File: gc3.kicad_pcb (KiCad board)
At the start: 6 copper layers, 99.1 x 66.8 mm, 191 parts, among them J1 JACK, J2 DM3AT-SF-PEJM5, P1 TESTPOINT, P10 UART1, P11 GND, P12 GND, P13 GND, P14 GND, P15 TESTPOINT, P16 TEESTPOINT, P17 GPIO, P18 USB_A, P19 USB_OTG, P2 TESTPOINT, P3 TESTPOINT, P4 TESTPOINT, P5 TESTPOINT, P6 TESTPOINT, P7 LCD, P8 JTAG, P9 UART0, SW1 PWR_ON, SW2 RESET, SW3 UBOOT, U1 TPS62290, U2 axp209, U3 TPS62290, U4 a13, U5 h5tq2g63bfr, U6 TPS2552, U8 TPS2552, Y1 24MHz/20pF/20ppm

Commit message: Add : finish Update$
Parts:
- C29, C30, C32, C33, C34, C35, C36, C38, C39, C40, C41, C42, C43, C44, C47, C48, C49, C66, C80, C81: footprint COMMON0603:Common_0603 -> Capacitors_SMD:C_0402
- C50: footprint COMMON0603:Common_0603 -> Capacitors_SMD:C_0402; moved to B.Cu
- C82: moved to B.Cu
- R19, R26, R66, R74: footprint COMMON0603:Common_0603 -> Resistors_SMD:R_0402
- moved R19 7.04 mm to (163.1, 109.0)
- moved C80 6.78 mm to (163.0, 107.6)
- moved R74 6.69 mm to (163.1, 106.3)
- moved C81 6.47 mm to (163.0, 105.0)
- moved C66 6.34 mm to (163.0, 103.7)
- moved C50 4.40 mm to (174.9, 83.4), turned to 180 degrees
- moved C35 4.25 mm to (152.7, 91.0)
- moved P15 3.86 mm to (144.7, 78.7)
- moved P16 3.60 mm to (124.0, 119.4)
- moved C1 3.35 mm to (123.0, 115.6)
- moved C33 2.34 mm to (148.8, 90.0)
- moved P14 2.04 mm to (129.1, 121.4)
- moved C72 2.00 mm to (166.2, 111.5), turned to 270 degrees
- moved C30 1.57 mm to (173.3, 68.7)
- moved C34 1.44 mm to (152.6, 87.8)
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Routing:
- net +5V: track 38.4 -> 170.0 mm
- net +1.5V: track 51.1 -> 109.5 mm, vias 17 -> 23
- net +3V3: track 47.5 -> 72.4 mm, vias 0 -> 19
- net GND: track 225.9 -> 244.1 mm, vias 102 -> 113
- net +3.0VA: track 72.0 -> 86.8 mm, vias 3 -> 4
- net IPSOUT: track 125.6 -> 137.1 mm, vias 14 -> 15
- net 1.2V_INT: track 30.6 -> 38.5 mm, vias 0 -> 7
- net /mpu_ddr3/SVREF: track 18.5 -> 11.2 mm
- net /mpu_ddr3/PIN39/USBH_EN: track 131.0 -> 123.7 mm
- net /mpu_ddr3/PIN8: track 80.2 -> 84.4 mm
- net /mpu_ddr3/DQS1_N: track 15.9 -> 11.8 mm
- net /mpu_ddr3/D15: track 14.2 -> 11.3 mm
- net /mpu_ddr3/A4: track 16.8 -> 19.3 mm
- net Net-(D2-Pad2): track 0.00 -> 2.58 mm
- net /mpu_ddr3/CK_N: track 22.1 -> 20.0 mm
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
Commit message: Commit before production Update4
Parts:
- added ?: , via:via, F.Cu at (185.6, 64.9)
- added ?: , via:via, F.Cu at (141.4, 84.9)
- added ?: , via:via, F.Cu at (109.1, 63.1)
- added ?: , via:via, F.Cu at (109.1, 58.9)
- added ?: , via:via, F.Cu at (112.4, 58.9)
- added ?: , via:via, F.Cu at (115.7, 58.9)
- added ?: , via:via, F.Cu at (118.7, 58.8)
- added ?: , via:via, F.Cu at (122.2, 58.8)
- added ?: , via:via, F.Cu at (128.1, 58.8)
- added ?: , via:via, F.Cu at (133.1, 67.0)
- added ?: , via:via, F.Cu at (131.3, 63.0)
- added ?: , via:via, F.Cu at (132.4, 58.8)
- added ?: , via:via, F.Cu at (137.0, 84.3)
- added ?: , via:via, F.Cu at (144.1, 65.0)
- added ?: , via:via, F.Cu at (137.0, 58.8)
- added ?: , via:via, F.Cu at (146.7, 58.8)
- added ?: , via:via, F.Cu at (144.3, 112.4)
- added ?: , via:via, F.Cu at (144.3, 107.1)
- added ?: , via:via, F.Cu at (155.1, 115.3)
- added ?: , via:via, F.Cu at (155.0, 112.1)
- added ?: , via:via, F.Cu at (158.9, 110.4)
- added ?: , via:via, F.Cu at (151.9, 114.1)
- added ?: , via:via, F.Cu at (152.0, 111.9)
- added ?: , via:via, F.Cu at (134.6, 107.1)
- added ?: , via:via, F.Cu at (151.9, 109.6)
- added ?: , via:via, F.Cu at (144.4, 108.9)
- added ?: , via:via, F.Cu at (162.7, 101.2)
- added ?: , via:via, F.Cu at (160.5, 103.5)
- added ?: , via:via, F.Cu at (159.4, 105.6)
- added ?: , via:via, F.Cu at (155.1, 104.5)
- added ?: , via:via, F.Cu at (155.1, 107.1)
- added ?: , via:via, F.Cu at (151.9, 107.2)
- added ?: , via:via, F.Cu at (188.8, 117.8)
- added ?: , via:via, F.Cu at (192.8, 119.3)
- added ?: , via:via, F.Cu at (135.3, 99.7)
- added ?: , via:via, F.Cu at (193.3, 121.7)
- added ?: , via:via, F.Cu at (192.7, 124.0)
- added ?: , via:via, F.Cu at (197.8, 121.0)
- added ?: , via:via, F.Cu at (192.3, 117.2)
- added ?: , via:via, F.Cu at (185.4, 113.6)
- added ?: , via:via, F.Cu at (190.3, 112.0)
- added ?: , via:via, F.Cu at (198.3, 115.2)
- added ?: , via:via, F.Cu at (201.4, 108.2)
- added ?: , via:via, F.Cu at (195.3, 108.6)
- added ?: , via:via, F.Cu at (189.1, 105.7)
- added ?: , via:via, F.Cu at (143.7, 99.7)
- added ?: , via:via, F.Cu at (192.4, 102.0)
- added ?: , via:via, F.Cu at (199.2, 103.2)
- added ?: , via:via, F.Cu at (206.7, 124.0)
- added ?: , via:via, F.Cu at (206.5, 121.7)
- added ?: , via:via, F.Cu at (206.5, 117.4)
- added ?: , via:via, F.Cu at (206.5, 112.8)
- added ?: , via:via, F.Cu at (206.6, 108.0)
- added ?: , via:via, F.Cu at (206.6, 101.4)
- added ?: , via:via, F.Cu at (202.6, 97.9)
- added ?: , via:via, F.Cu at (195.4, 97.3)
- added ?: , via:via, F.Cu at (168.6, 102.0)
- added ?: , via:via, F.Cu at (188.2, 97.6)
- added ?: , via:via, F.Cu at (176.9, 77.3)
- added ?: , via:via, F.Cu at (183.9, 113.3)
- added ?: , via:via, F.Cu at (185.1, 95.4)
- added ?: , via:via, F.Cu at (185.1, 89.1)
- added ?: , via:via, F.Cu at (151.2, 58.9)
- added ?: , via:via, F.Cu at (177.9, 83.4)
- added ?: , via:via, F.Cu at (185.1, 92.0)
- added ?: , via:via, F.Cu at (185.1, 98.5)
- added ?: , via:via, F.Cu at (185.3, 84.9)
- added ?: , via:via, F.Cu at (134.4, 114.9)
- added ?: , via:via, F.Cu at (188.0, 87.6)
- added ?: , via:via, F.Cu at (190.9, 96.1)
- added ?: , via:via, F.Cu at (199.3, 94.8)
- added ?: , via:via, F.Cu at (206.6, 94.7)
- added ?: , via:via, F.Cu at (190.1, 83.3)
- added ?: , via:via, F.Cu at (206.6, 72.1)
- added ?: , via:via, F.Cu at (206.6, 79.3)
- added ?: , via:via, F.Cu at (202.0, 79.1)
- added ?: , via:via, F.Cu at (197.3, 79.4)
- added ?: , via:via, F.Cu at (193.0, 77.4)
- added ?: , via:via, F.Cu at (133.8, 111.5)
- added ?: , via:via, F.Cu at (206.6, 87.5)
- added ?: , via:via, F.Cu at (199.3, 75.2)
- added ?: , via:via, F.Cu at (204.8, 75.7)
- added ?: , via:via, F.Cu at (203.3, 72.0)
- added ?: , via:via, F.Cu at (200.7, 67.8)
- added ?: , via:via, F.Cu at (194.5, 70.2)
- added ?: , via:via, F.Cu at (190.0, 70.0)
- added ?: , via:via, F.Cu at (154.1, 58.9)
- added ?: , via:via, F.Cu at (190.4, 66.5)
- added ?: , via:via, F.Cu at (191.8, 64.1)
- added ?: , via:via, F.Cu at (132.9, 112.2)
- added ?: , via:via, F.Cu at (191.7, 60.9)
- added ?: , via:via, F.Cu at (194.9, 62.4)
- added ?: , via:via, F.Cu at (182.7, 58.9)
- added ?: , via:via, F.Cu at (197.9, 58.8)
- added ?: , via:via, F.Cu at (193.7, 58.8)
- added ?: , via:via, F.Cu at (202.9, 58.7)
- added ?: , via:via, F.Cu at (199.7, 63.3)
- added ?: , via:via, F.Cu at (206.3, 63.5)
- added ?: , via:via, F.Cu at (176.9, 98.5)
- added ?: , via:via, F.Cu at (206.7, 58.7)
- added ?: , via:via, F.Cu at (135.6, 111.8)
- added ?: , via:via, F.Cu at (188.5, 68.5)
- added ?: , via:via, F.Cu at (182.8, 64.8)
- added ?: , via:via, F.Cu at (143.6, 103.8)
- added ?: , via:via, F.Cu at (137.4, 107.2)
- added ?: , via:via, F.Cu at (141.3, 107.2)
- added ?: , via:via, F.Cu at (141.6, 111.6)
- added ?: , via:via, F.Cu at (138.5, 108.8)
- added ?: , via:via, F.Cu at (142.9, 113.8)
- added ?: , via:via, F.Cu at (140.9, 118.0)
- added ?: , via:via, F.Cu at (132.8, 120.0)
- added ?: , via:via, F.Cu at (131.0, 115.8)
- added ?: , via:via, F.Cu at (126.9, 117.3)
- added ?: , via:via, F.Cu at (180.6, 67.0)
- added ?: , via:via, F.Cu at (125.0, 110.7)
- added ?: , via:via, F.Cu at (127.9, 111.4)
- added ?: , via:via, F.Cu at (128.0, 107.1)
- added ?: , via:via, F.Cu at (126.0, 107.2)
- added ?: , via:via, F.Cu at (123.6, 107.1)
- added ?: , via:via, F.Cu at (121.8, 118.0)
- added ?: , via:via, F.Cu at (135.2, 123.9)
- added ?: , via:via, F.Cu at (131.2, 123.9)
- added ?: , via:via, F.Cu at (124.1, 123.9)
- added ?: , via:via, F.Cu at (119.7, 123.9)
- added ?: , via:via, F.Cu at (183.4, 67.0)
- added ?: , via:via, F.Cu at (114.7, 123.9)
- added ?: , via:via, F.Cu at (112.5, 119.2)
- added ?: , via:via, F.Cu at (115.7, 117.7)
- added ?: , via:via, F.Cu at (113.9, 113.3)
- added ?: , via:via, F.Cu at (112.8, 110.4)
- added ?: , via:via, F.Cu at (111.3, 106.5)
- added ?: , via:via, F.Cu at (109.2, 123.9)
- added ?: , via:via, F.Cu at (109.1, 121.4)
- added ?: , via:via, F.Cu at (109.1, 117.5)
- added ?: , via:via, F.Cu at (109.1, 114.2)
- added ?: , via:via, F.Cu at (136.4, 90.4)
- added ?: , via:via, F.Cu at (109.1, 110.1)
- added ?: , via:via, F.Cu at (120.6, 91.1)
- added ?: , via:via, F.Cu at (112.7, 96.0)
- added ?: , via:via, F.Cu at (109.2, 95.4)
- added ?: , via:via, F.Cu at (109.2, 93.8)
- added ?: , via:via, F.Cu at (111.2, 89.1)
- added ?: , via:via, F.Cu at (109.1, 89.2)
- added ?: , via:via, F.Cu at (109.1, 86.4)
- added ?: , via:via, F.Cu at (111.4, 78.8)
- added ?: , via:via, F.Cu at (111.4, 73.0)
- added ?: , via:via, F.Cu at (142.3, 94.5)
- added ?: , via:via, F.Cu at (109.2, 79.6)
- added ?: , via:via, F.Cu at (109.1, 74.7)
- added ?: , via:via, F.Cu at (109.1, 70.1)
- added ?: , via:via, F.Cu at (113.0, 71.2)
- added ?: , via:via, F.Cu at (113.0, 66.9)
- added ?: , via:via, F.Cu at (111.7, 65.7)
- added ?: , via:via, F.Cu at (109.1, 66.3)
- added ?: , via:via, F.Cu at (125.2, 82.1)
- added ?: , via:via, F.Cu at (114.6, 87.5)
- added ?: , via:via, F.Cu at (113.9, 87.6)
- added ?: , via:via, F.Cu at (139.6, 94.5)
- added ?: , via:via, F.Cu at (113.8, 82.0)
- added ?: , via:via, F.Cu at (115.6, 83.7)
- added ?: , via:via, F.Cu at (117.9, 83.8)
- added ?: , via:via, F.Cu at (120.9, 84.5)
- added ?: , via:via, F.Cu at (127.1, 86.2)
- added ?: , via:via, F.Cu at (123.3, 83.2)
- added ?: , via:via, F.Cu at (120.1, 81.3)
- added ?: , via:via, F.Cu at (116.8, 81.3)
- added ?: , via:via, F.Cu at (125.1, 79.1)
- added ?: , via:via, F.Cu at (129.6, 79.1)
- added ?: , via:via, F.Cu at (143.2, 88.9)
- added ?: , via:via, F.Cu at (129.7, 74.5)
- added ?: , via:via, F.Cu at (128.2, 71.4)
- added ?: , via:via, F.Cu at (137.5, 75.3)
- added ?: , via:via, F.Cu at (137.7, 76.2)
- added ?: , via:via, F.Cu at (140.9, 74.8)
- added ?: , via:via, F.Cu at (145.5, 74.5)
- added ?: , via:via, F.Cu at (143.7, 72.2)
- added ?: , via:via, F.Cu at (143.7, 69.0)
- added ?: , via:via, F.Cu at (141.9, 68.4)
- added ?: , via:via, F.Cu at (149.9, 69.5)
- added ?: , via:via, F.Cu at (145.2, 86.8)
- added ?: , via:via, F.Cu at (147.2, 70.1)
- added ?: , via:via, F.Cu at (146.1, 71.9)
- added ?: , via:via, F.Cu at (139.2, 71.5)
- added ?: , via:via, F.Cu at (131.5, 69.2)
- added ?: , via:via, F.Cu at (123.5, 69.2)
- added ?: , via:via, F.Cu at (128.1, 66.1)
- added ?: , via:via, F.Cu at (121.3, 64.9)
- added ?: , via:via, F.Cu at (119.4, 61.6)
- added ?: , via:via, F.Cu at (114.9, 70.4)
- added ?: , via:via, F.Cu at (114.3, 63.3)
- moved C66 3.03 mm to (163.1, 106.7)
- moved R66 2.91 mm to (162.8, 105.0)
- moved C81 2.74 mm to (163.1, 107.7)
- moved R74 2.41 mm to (163.2, 108.7)
- moved C80 2.07 mm to (163.1, 109.7)
- moved R19 1.70 mm to (163.2, 110.7)
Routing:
- net GND: track 244.1 -> 298.2 mm, vias 113 -> 122
- net /mpu_ddr3/DQS1_N: track 11.8 -> 16.0 mm
- net /mpu_ddr3/DM0: track 12.4 -> 16.1 mm
- net /mpu_ddr3/BA1: track 15.6 -> 19.0 mm
- net /mpu_ddr3/DM1: track 11.5 -> 14.5 mm
- net Net-(R66-Pad2): track 4.43 -> 7.18 mm
- net /mpu_ddr3/A4: track 19.3 -> 16.7 mm
- net +1.5V: track 109.5 -> 107.2 mm
- net /mpu_ddr3/SVREF: track 11.2 -> 12.9 mm
- net +3V3: track 72.4 -> 70.9 mm
- net /mpu_ddr3/DQS1_P: track 15.1 -> 16.1 mm
- net /mpu_ddr3/PIN13/NALE: track 23.9 -> 24.8 mm
- net /mpu_ddr3/PIN14/NCLE: track 23.4 -> 24.3 mm
- net /mpu_ddr3/PIN12/NWE: track 25.3 -> 26.2 mm
- net /EXTEN: track 24.2 -> 23.4 mm
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- added copper zone on In1.Cu, net GND
- added copper zone on In2.Cu, net GND

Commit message: temp : commit before change 8 layer
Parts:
- moved C30 1.93 mm to (171.8, 69.8)
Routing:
- net GND: track 298.2 -> 329.0 mm, vias 122 -> 125
- net +3V3: track 70.9 -> 67.0 mm
- net PIN5/TWI0-SDA: track 125.2 -> 121.7 mm
- net Net-(R4-Pad2): track 35.2 -> 34.4 mm
- net Net-(R1-Pad1): track 53.5 -> 52.8 mm
- net /mpu_ddr3/PIN27/NDQ7: track 47.8 -> 48.4 mm

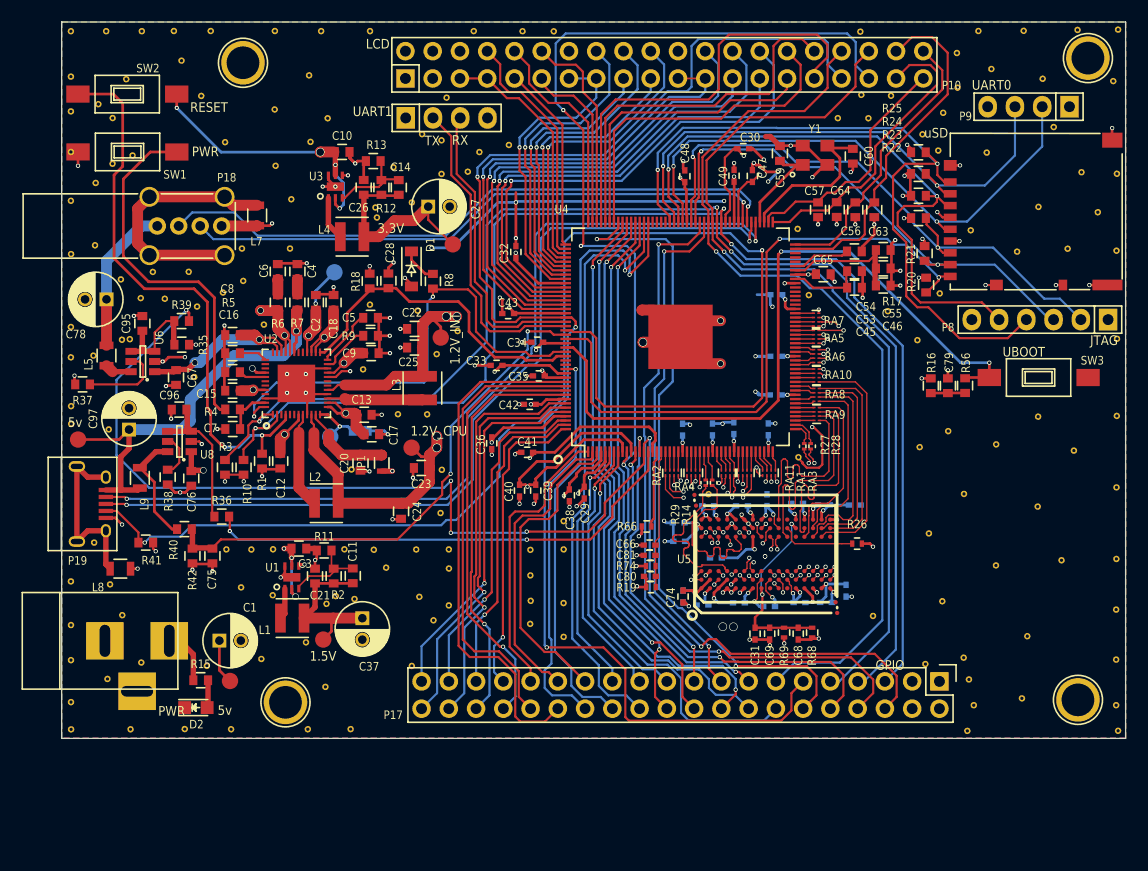
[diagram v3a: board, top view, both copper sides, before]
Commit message: Fix : fix line width for impedance matching
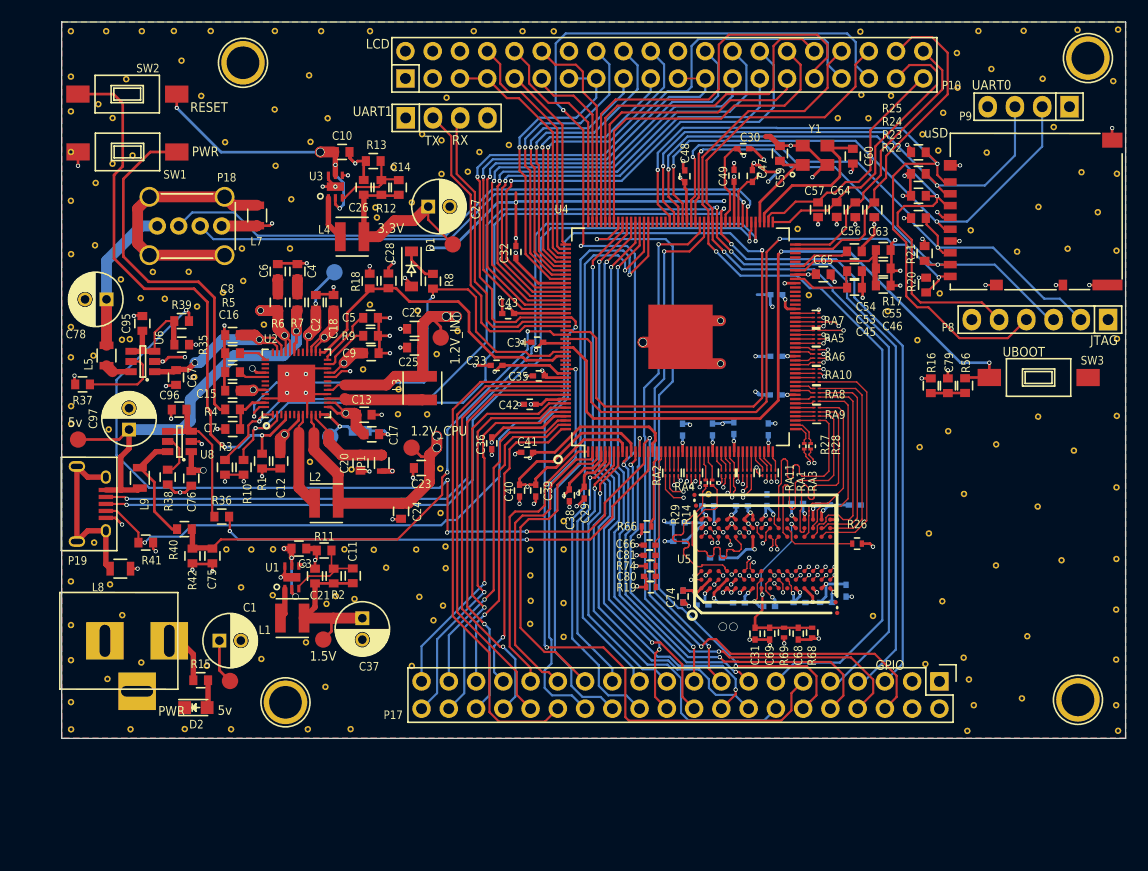
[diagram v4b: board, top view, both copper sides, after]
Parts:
- removed the ? at (143.7, 99.7)
- removed the ? at (176.9, 98.5)
- added ?: , via:via, F.Cu at (139.7, 92.2)
- added ?: , via:via, F.Cu at (131.4, 99.0)
- added ?: , via:via, F.Cu at (143.6, 99.6)
- C34, C43: value 22uF/6.3V -> 0.1uF/6.3V
- C42, C49: value 0.1uF/6.3V -> 22uF/6.3V
- J1: footprint Connect:BARREL_JACK -> MyConnector:BARREL_JACK
- P18: footprint Connect:USB_A_Vertical -> MyConnector:USB_A_Vertical
- P19: footprint Connect:USB_Micro-B -> MyConnector:USB_Micro-B
- moved ? 0.54 mm to (143.8, 112.4)
- moved ? 0.41 mm to (144.0, 106.9)
- moved ? 0.30 mm to (144.1, 108.9)
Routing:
- net GND: track 329.0 -> 278.9 mm, vias 125 -> 121
- net +1.5V: track 107.2 -> 108.8 mm
- net +3.0VA: track 86.8 -> 88.2 mm
- net /mpu_ddr3/DQS1_P: track 16.1 -> 15.0 mm
- net /mpu_ddr3/DQS1_N: track 16.0 -> 15.0 mm
- net /mpu_ddr3/PIN26/NDQ6: track 42.3 -> 41.4 mm
- removed copper zone on In1.Cu, net GND
- removed copper zone on In2.Cu, net GND
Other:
- net class Thin added: clearance 0.1, trace_width 0.1, via_dia 0.4, via_drill 0.25
